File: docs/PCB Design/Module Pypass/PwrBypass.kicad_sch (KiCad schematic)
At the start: 4 parts, among them J11 Conn_02x05_Top_Bottom, J14 Conn_02x04_Counter_Clockwise

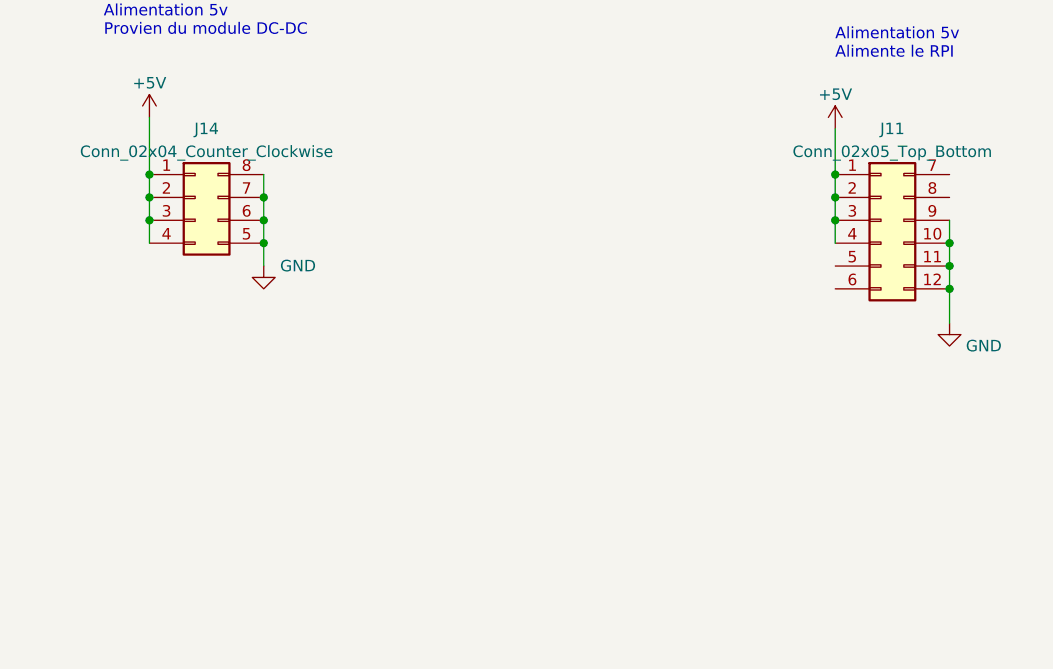
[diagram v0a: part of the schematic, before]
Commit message: module power 1.0 module bypass 1.1
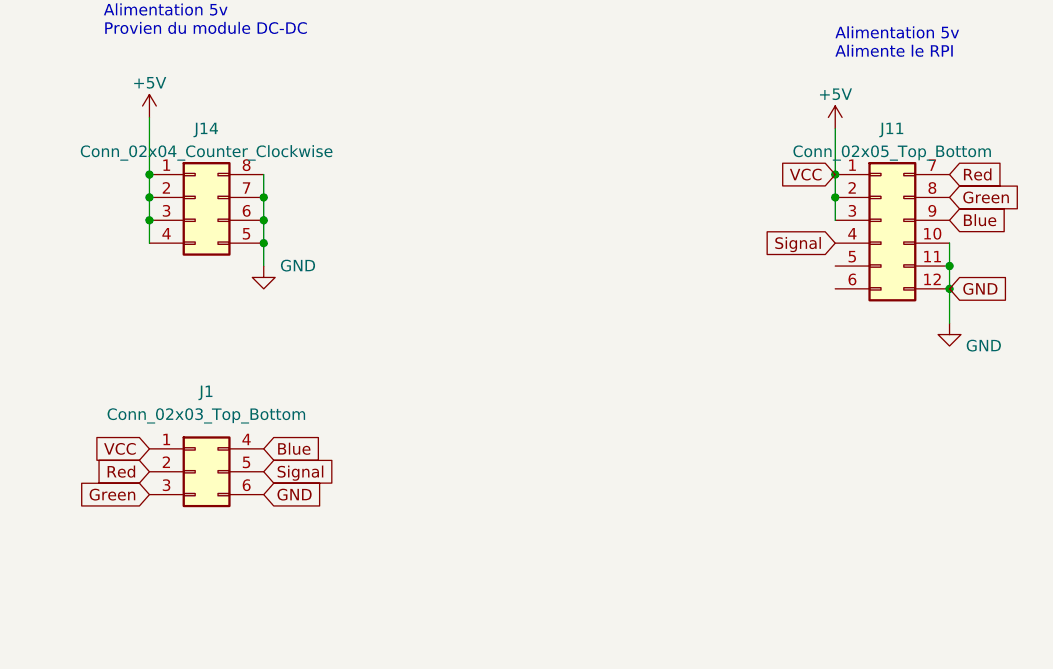
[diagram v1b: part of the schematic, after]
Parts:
- added J1: Conn_02x03_Top_Bottom, Connector_IDC:IDC-Header_2x03_P2.54mm_Vertical, symbol Connector_Generic:Conn_02x03_Top_Bottom
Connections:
- net +5V: now also J1.1 (Pin_1); no longer J11.4 (Pin_4)
- net GND: now also J1.6 (Pin_6); no longer J11.9 (Pin_9)
- net Red: now reaches J11.7 (Pin_7)
- net Red: now also J1.2 (Pin_2)
- net Green: now reaches J11.8 (Pin_8)
- net Green: now also J1.3 (Pin_3)
- new net Blue: J1.4 (Pin_4), J11.9 (Pin_9)
- new net Signal: J1.5 (Pin_5), J11.4 (Pin_4)
